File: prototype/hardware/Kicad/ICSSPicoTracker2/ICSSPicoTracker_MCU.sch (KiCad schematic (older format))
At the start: 21 parts, among them J1 Conn_01x04, J2 Conn_01x02, U1 ATSAML21E18B-MUT, U2 W25Q32JVSS, U3 NCP303

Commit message: Add GPS, Remove FM
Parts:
- removed C?: 100nf, Capacitor_SMD:C_0603_1608Metric, symbol Device:C
- removed R? (x3): 10k, symbol Device:R
- removed U?: Si5351B-B-GM, Package_DFN_QFN:QFN-20-1EP_4x4mm_P0.5mm_EP2.7x2.7mm, symbol Oscillator:Si5351B-B-GM
- removed U?: MCP601-xOT, Package_TO_SOT_SMD:SOT-23-5, symbol Amplifier_Operational:MCP601-xOT
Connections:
- net labels removed: +3.3V, DAC-SAM, GPS-TCXO, RF-CLK
- wire segments 124 -> 85

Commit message: Updated Scehematics and Footprints
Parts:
- removed U1: ATSAML21E18B-MUT, Package_DFN_QFN:QFN-32-1EP_5x5mm_P0.5mm_EP3.45x3.45mm, symbol ICSSPicoTracker:ATSAML21E18B-MUT
- removed U2: W25Q32JVSS, Package_SO:SOIC-8_5.23x5.23mm_P1.27mm, symbol Memory_Flash:W25Q32JVSS
- removed U3: NCP303, Package_TO_SOT_SMD:SOT-23-5, symbol ICSSPicoTracker:NCP303
- added C86, C88: 15pF, Capacitor_SMD:C_0402_1005Metric, symbol Device:C
- added C87: 22pF, Capacitor_SMD:C_0402_1005Metric, symbol Device:C
- added C89, C91, C93: 100nF, Capacitor_SMD:C_0603_1608Metric, symbol Device:C
- added C90: 1uF, Capacitor_SMD:C_0603_1608Metric, symbol Device:C
- added C92: https://www.murata.com/en-eu/products/productdata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, Capacitor_SMD:C_0603_1608Metric, symbol Device:C
- added R12: 1K, Resistor_SMD:R_0603_1608Metric, symbol Device:R
- added U1: ATSAML21G18B-MUT, Package_DFN_QFN:QFN-48-1EP_7x7mm_P0.5mm_EP5.15x5.15mm, symbol MCU_Microchip_SAML:ATSAML21G18B-MUT
- added U2: W25Q16DW, Package_SON:WSON-8-1EP_6x5mm_P1.27mm_EP3.4x4.3mm, symbol ICSSPicoTracker:W25Q16DW
- added Y2: 32.768KHz, Crystal:Crystal_SMD_2012-2Pin_2.0x1.2mm, symbol Device:Crystal
- added Y3: 16MHz, Crystal:Crystal_SMD_2520-4Pin_2.5x2.0mm, symbol Device:Crystal
- C1, C2: value 10uf -> https://www.murata.com/en-eu/products/productdata/8797690593310/DS-SAFEB1G57KE0F00.pdf?1453347007000; footprint (none) -> Capacitor_SMD:C_0603_1608Metric
- C3, C4, C7: value 100nf -> 100nF; footprint (none) -> Capacitor_SMD:C_0603_1608Metric
- C5: value 10uf -> https://www.murata.com/en-eu/products/productdata/8797690593310/DS-SAFEB1G57KE0F00.pdf?1453347007000
- C6: value 100nf -> 100nF
- C9: value 100nf -> 22pF; footprint (none) -> Capacitor_SMD:C_0402_1005Metric
- J1: footprint (none) -> Connector_PinHeader_1.00mm:PinHeader_1x04_P1.00mm_Vertical
- J2: footprint (none) -> Connector_PinHeader_1.00mm:PinHeader_1x02_P1.00mm_Vertical
- L1: footprint (none) -> Inductor_SMD:L_0603_1608Metric
- R1: value 10k -> 1K; footprint (none) -> Resistor_SMD:R_0603_1608Metric
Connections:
- net labels added: MCU_MISO1, MCU_MISO4, MCU_MOSI1, MCU_MOSI4, MCU_NSEL1, MCU_NSEL4, MCU_PA02, MCU_PA03, MCU_PA04, MCU_PA05, MCU_PA06, MCU_PA07, MCU_PA08, MCU_PA09, MCU_PA13, MCU_PB02, MCU_PB03, MCU_PB08, MCU_RXD0, MCU_SCL3, MCU_SCLK1, MCU_SCLK4, MCU_SDA3, MCU_TXD0, USB_DM, USB_DP, XIN, XIN32, XOUT, XOUT32
- net labels removed: ADC-BAT, CS-RADIO, EN-GPS, EN3V-PSU, GPS-1PPS, MISO-SAM, MOSI-SAM, RXD-GPS, SAM-CLK, SCK-SAM, SCL-SAM, SDA-SAM, TXD-GPS, USB-DM, USB-DP
- wire segments 85 -> 150
- no-connect marks 7 -> 6
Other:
- moved on the sheet: C1, C2, C3, C4, C5, C6, C7, J1, J2, L1, R1

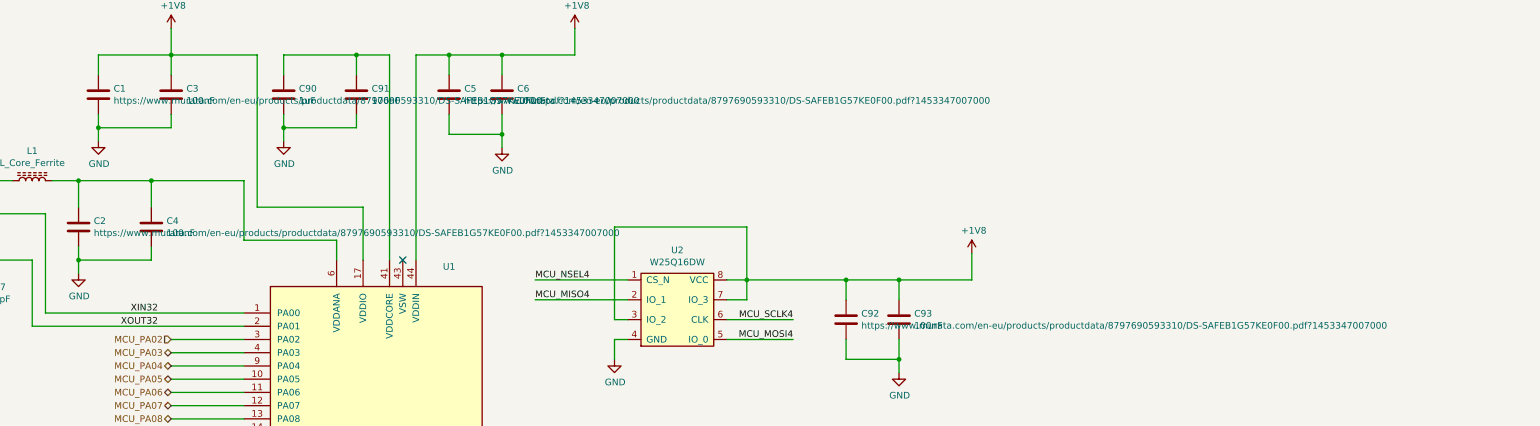
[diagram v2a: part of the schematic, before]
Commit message: Add Antenna footprints
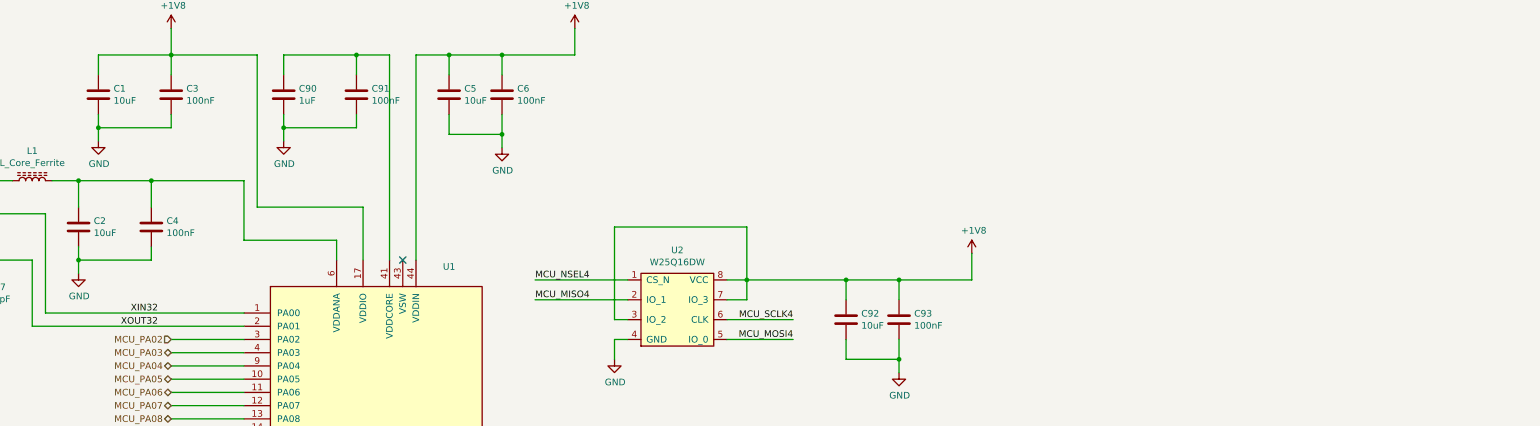
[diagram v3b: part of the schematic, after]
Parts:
- C1, C2, C5, C92: value https://www.murata.com/en-eu/products/productdata/8797690593310/DS-SAFEB1G57KE0F00.pdf?1453347007000 -> 10uF
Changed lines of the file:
@@
 P 3850 2250
 F 0 "C2" H 3965 2296 50  0000 L CNN
-F 1 "https://www.murata.com/en-eu/products/productdata/8797690593310/DS-SAFEB1G57KE0F00.pdf?1453347007000" H 3965 2205 50  0000 L CNN
+F 1 "10uF" H 3965 2205 50  0000 L CNN
 F 2 "Capacitor_SMD:C_0603_1608Metric" H 3888 2100 50  0001 C CNN
 F 3 "~" H 3850 2250 50  0001 C CNN
@@
 P 4000 1250
 F 0 "C1" H 4115 1296 50  0000 L CNN
-F 1 "https://www.murata.com/en-eu/products/productdata/8797690593310/DS-SAFEB1G57KE0F00.pdf?1453347007000" H 4115 1205 50  0000 L CNN
+F 1 "10uF" H 4115 1205 50  0000 L CNN
 F 2 "Capacitor_SMD:C_0603_1608Metric" H 4038 1100 50  0001 C CNN
 F 3 "~" H 4000 1250 50  0001 C CNN
@@
 P 6650 1250
 F 0 "C5" H 6765 1296 50  0000 L CNN
-F 1 "https://www.murata.com/en-eu/products/productdata/8797690593310/DS-SAFEB1G57KE0F00.pdf?1453347007000" H 6765 1205 50  0000 L CNN
+F 1 "10uF" H 6765 1205 50  0000 L CNN
 F 2 "Capacitor_SMD:C_0603_1608Metric" H 6688 1100 50  0001 C CNN
 F 3 "~" H 6650 1250 50  0001 C CNN
@@
 P 9650 2950
 F 0 "C92" H 9765 2996 50  0000 L CNN
-F 1 "https://www.murata.com/en-eu/products/productdata/8797690593310/DS-SAFEB1G57KE0F00.pdf?1453347007000" H 9765 2905 50  0000 L CNN
+F 1 "10uF" H 9765 2905 50  0000 L CNN
 F 2 "Capacitor_SMD:C_0603_1608Metric" H 9688 2800 50  0001 C CNN
 F 3 "~" H 9650 2950 50  0001 C CNN

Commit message: Some more ERC fixes
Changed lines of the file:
@@
 $EndComp
 Wire Wire Line
-	3650 1900 3850 1900
+	3650 1900 3800 1900
 Wire Wire Line
 	7600 950  7600 750
@@
 L power:GND #PWR089
 U 1 1 5D6856C6
-P 5400 1600
-F 0 "#PWR089" H 5400 1350 50  0001 C CNN
-F 1 "GND" H 5405 1427 50  0000 C CNN
-F 2 "" H 5400 1600 50  0001 C CNN
-F 3 "" H 5400 1600 50  0001 C CNN
-	1    5400 1600
+P 5400 1650
+F 0 "#PWR089" H 5400 1400 50  0001 C CNN
+F 1 "GND" H 5405 1477 50  0000 C CNN
+F 2 "" H 5400 1650 50  0001 C CNN
+F 3 "" H 5400 1650 50  0001 C CNN
+	1    5400 1650
 	1    0    0    -1
 $EndComp
@@
 $EndComp
 Wire Wire Line
-	5400 1600 5400 1500
-Wire Wire Line
 	5950 1400 5950 1500
 Wire Wire Line
@@
 Connection ~ 6650 950
 Wire Wire Line
-	6200 950  5950 950
+	6200 950  6100 950
 Connection ~ 5950 950
 Connection ~ 4550 950
@@
 Text Label 4550 4100 0    50   ~ 0
 MCU_MISO4
+$Comp
+L power:PWR_FLAG #FLG0101
+U 1 1 5D614102
+P 3800 1900
+F 0 "#FLG0101" H 3800 1975 50  0001 C CNN
+F 1 "PWR_FLAG" H 3800 2073 50  0000 C CNN
+F 2 "" H 3800 1900 50  0001 C CNN
+F 3 "~" H 3800 1900 50  0001 C CNN
+	1    3800 1900
+	1    0    0    -1
+$EndComp
+Connection ~ 3800 1900
+Wire Wire Line
+	3800 1900 3850 1900
+$Comp
+L power:PWR_FLAG #FLG0102
+U 1 1 5D621597
+P 6100 950
+F 0 "#FLG0102" H 6100 1025 50  0001 C CNN
+F 1 "PWR_FLAG" H 6100 1123 50  0000 C CNN
+F 2 "" H 6100 950 50  0001 C CNN
+F 3 "~" H 6100 950 50  0001 C CNN
+	1    6100 950
+	1    0    0    -1
+$EndComp
+Connection ~ 6100 950
+Wire Wire Line
+	6100 950  5950 950
+Wire Wire Line
+	5400 1500 5400 1650
 $EndSCHEMATC

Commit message: fully wired up the LD3985 LDO
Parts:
- U2: symbol ICSSPicoTracker:W25Q16DW -> ICSSPicoTracker2-rescue:W25Q16DW-ICSSPicoTracker-ICSSPicoTracker2-rescue
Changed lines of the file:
@@
 MCU_PA02
 $Comp
-L ICSSPicoTracker:W25Q16DW U2
+L ICSSPicoTracker2-rescue:W25Q16DW-ICSSPicoTracker-ICSSPicoTracker2-rescue U2
 U 1 1 5D77FBCE
 P 8100 3150

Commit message: Revert "fully wired up the LD3985 LDO"
This reverts commit 04a440f3a08b8c97db9d4cc44cd5207f890db50a.
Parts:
- U2: symbol ICSSPicoTracker2-rescue:W25Q16DW-ICSSPicoTracker-ICSSPicoTracker2-rescue -> ICSSPicoTracker:W25Q16DW
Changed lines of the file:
@@
 MCU_PA02
 $Comp
-L ICSSPicoTracker2-rescue:W25Q16DW-ICSSPicoTracker-ICSSPicoTracker2-rescue U2
+L ICSSPicoTracker:W25Q16DW U2
 U 1 1 5D77FBCE
 P 8100 3150
